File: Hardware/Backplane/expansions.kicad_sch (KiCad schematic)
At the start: 3 parts, among them U101 P2X8C4M64P, U102 TCA9548APWR

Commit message: Adjusts to review comments
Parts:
- C101: Digikey Part No (none) -> 399-C0603C104M4RACTUCT-ND
- renumbered U101 to U2901
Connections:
- net I2C1_{SCL}: now also U102.5 (SC0); no longer U102.7 (SC1)
- net I2C1_{SDA}: now also U102.4 (SD0); no longer U102.6 (SD1)
- net I2C2_{SCL}: now also U102.7 (SC1); no longer U102.9 (SC2)
- net I2C2_{SDA}: now also U102.6 (SD1); no longer U102.8 (SD2)
- net I2C3_{SCL}: now also U102.9 (SC2); no longer U102.11 (SC3)
- net I2C3_{SDA}: now also U102.8 (SD2); no longer U102.10 (SD3)
- net I2C4_{SCL}: now also U102.11 (SC3); no longer U102.14 (SC4)
- net I2C4_{SDA}: now also U102.10 (SD3); no longer U102.13 (SD4)
- net I2C5_{SCL}: now also U102.14 (SC4); no longer U102.16 (SC5)
- net I2C5_{SDA}: now also U102.13 (SD4); no longer U102.15 (SD5)
- net I2C6_{SCL}: now also U102.16 (SC5); no longer U102.18 (SC6)
- net I2C6_{SDA}: now also U102.15 (SD5); no longer U102.17 (SD6)
- net I2C7_{SCL}: now also U102.18 (SC6); no longer U102.20 (SC7)
- net I2C7_{SDA}: now also U102.17 (SD6); no longer U102.19 (SD7)
- net I2C^{BRD}_{SCL}: now also U102.19 (SD7); no longer U102.4 (SD0)
- net I2C^{BRD}_{SDA}: now also U102.20 (SC7); no longer U102.5 (SC0)
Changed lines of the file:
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@@
 	(wire
 		(pts
+			(xy 164.465 152.4) (xy 166.37 152.4)
+		)
+		(stroke
+			(width 0)
+			(type default)
+		)
+	)
+	(wire
+		(pts
 			(xy 37.465 73.66) (xy 37.465 72.39)
 		)
@@
 	(wire
 		(pts
-			(xy 166.37 119.38) (xy 155.575 119.38)
+			(xy 166.37 111.76) (xy 155.575 111.76)
 		)
 		(stroke
@@
 	(wire
 		(pts
-			(xy 166.37 134.62) (xy 155.575 134.62)
+			(xy 166.37 127) (xy 155.575 127)
 		)
 		(stroke
@@
 	(wire
 		(pts
-			(xy 166.37 152.4) (xy 155.575 152.4)
+			(xy 166.37 144.78) (xy 155.575 144.78)
 		)
 		(stroke
@@
 	(wire
 		(pts
-			(xy 166.37 114.3) (xy 155.575 114.3)
+			(xy 166.37 106.68) (xy 155.575 106.68)
 		)
 		(stroke
@@
 	(wire
 		(pts
-			(xy 166.37 127) (xy 155.575 127)
+			(xy 166.37 119.38) (xy 155.575 119.38)
 		)
 		(stroke
@@
 	(wire
 		(pts
-			(xy 166.37 144.78) (xy 155.575 144.78)
+			(xy 166.37 137.16) (xy 155.575 137.16)
 		)
 		(stroke
@@
 	(wire
 		(pts
-			(xy 166.37 149.86) (xy 155.575 149.86)
+			(xy 166.37 142.24) (xy 155.575 142.24)
 		)
 		(stroke
@@
 	(wire
 		(pts
+			(xy 164.465 149.86) (xy 166.37 149.86)
+		)
+		(stroke
+			(width 0)
+			(type default)
+		)
+	)
+	(wire
+		(pts
 			(xy 44.45 35.56) (xy 46.99 35.56)
 		)
@@
 	(wire
 		(pts
-			(xy 166.37 106.68) (xy 155.575 106.68)
+			(xy 166.37 99.06) (xy 155.575 99.06)
 		)
 		(stroke
@@
 	(wire
 		(pts
-			(xy 166.37 111.76) (xy 155.575 111.76)
+			(xy 166.37 104.14) (xy 155.575 104.14)
 		)
 		(stroke
@@
 	(wire
 		(pts
-			(xy 166.37 129.54) (xy 155.575 129.54)
+			(xy 166.37 121.92) (xy 155.575 121.92)
 		)
 		(stroke
@@
 	(wire
 		(pts
-			(xy 166.37 142.24) (xy 155.575 142.24)
+			(xy 166.37 134.62) (xy 155.575 134.62)
 		)
 		(stroke
@@
 	(wire
 		(pts
-			(xy 166.37 121.92) (xy 155.575 121.92)
+			(xy 166.37 114.3) (xy 155.575 114.3)
 		)
 		(stroke
@@
 	(wire
 		(pts
-			(xy 166.37 137.16) (xy 155.575 137.16)
+			(xy 166.37 129.54) (xy 155.575 129.54)
 		)
 		(stroke
@@
 	(wire
 		(pts
-			(xy 166.37 104.14) (xy 155.575 104.14)
+			(xy 166.37 96.52) (xy 155.575 96.52)
 		)
 		(stroke
@@
 	)
 	(label "I2C7_{SCL}"
-		(at 155.575 152.4 0)
+		(at 155.575 144.78 0)
 		(effects
 			(font
@@
 	)
 	(label "I2C7_{SDA}"
-		(at 155.575 149.86 0)
+		(at 155.575 142.24 0)
 		(effects
 			(font
@@
 	)
 	(label "I2C2_{SCL}"
-		(at 155.575 114.3 0)
+		(at 155.575 106.68 0)
 		(effects
 			(font
@@
 	)
 	(label "I2C6_{SCL}"
-		(at 155.575 144.78 0)
+		(at 155.575 137.16 0)
 		(effects
 			(font
@@
 	)
 	(label "I2C3_{SDA}"
-		(at 155.575 119.38 0)
+		(at 155.575 111.76 0)
 		(effects
 			(font
@@
 	)
 	(label "I2C1_{SCL}"
-		(at 155.575 106.68 0)
+		(at 155.575 99.06 0)
 		(effects
 			(font
@@
 	)
 	(label "I2C4_{SCL}"
-		(at 155.575 129.54 0)
+		(at 155.575 121.92 0)
 		(effects
 			(font
@@
 	)
 	(label "I2C3_{SCL}"
-		(at 155.575 121.92 0)
+		(at 155.575 114.3 0)
 		(effects
 			(font
@@
 	)
 	(label "I2C4_{SDA}"
-		(at 155.575 127 0)
+		(at 155.575 119.38 0)
 		(effects
 			(font
@@
 	)
 	(label "I2C2_{SDA}"
-		(at 155.575 111.76 0)
+		(at 155.575 104.14 0)
 		(effects
 			(font
@@
 	)
 	(label "I2C1_{SDA}"
-		(at 155.575 104.14 0)
+		(at 155.575 96.52 0)
 		(effects
 			(font
@@
 	)
 	(label "I2C6_{SDA}"
-		(at 155.575 142.24 0)
+		(at 155.575 134.62 0)
 		(effects
 			(font
@@
 	)
 	(label "I2C5_{SDA}"
-		(at 155.575 134.62 0)
+		(at 155.575 127 0)
 		(effects
 			(font
@@
 	)
 	(label "I2C5_{SCL}"
-		(at 155.575 137.16 0)
+		(at 155.575 129.54 0)
 		(effects
 			(font
@@
 	(global_label "I2C^{BRD}_{SDA}"
 		(shape input)
-		(at 166.37 99.06 180)
+		(at 164.465 152.4 180)
 		(fields_autoplaced yes)
 		(effects
@@
 		)
 		(property "Intersheetrefs" "${INTERSHEET_REFS}"
-			(at 154.3472 99.06 0)
+			(at 152.4422 152.4 0)
 			(effects
 				(font
@@
 	(global_label "I2C^{BRD}_{SCL}"
 		(shape input)
-		(at 166.37 96.52 180)
+		(at 164.465 149.86 180)
 		(fields_autoplaced yes)
 		(effects
@@
 		)
 		(property "Intersheetrefs" "${INTERSHEET_REFS}"
-			(at 154.3956 96.52 0)
+			(at 152.4906 149.86 0)
 			(effects
 				(font
@@
 		(on_board yes)
 		(dnp no)
-		(property "Reference" "U101"
+		(property "Reference" "U2901"
 			(at 251.46 17.78 0)
 			(effects
@@
 			(project "Backplane"
 				(path "/c6da991a-d3ed-4ac1-8b0d-12cd7ba8539b/fc524bed-e1de-43ff-9b23-75610ded7ea1"
-					(reference "U101")
+					(reference "U2901")
 					(unit 1)
 				)
@@
 			)
 		)
-		(property "Datasheet" ""
+		(property "Datasheet" "https://www.yageogroup.com/content/datasheet/asset/file/KEM_C1002_X7R_SMD"
 			(at 202.565 125.095 0)
 			(effects
@@
 			(at 202.565 125.095 0)
 			(effects
+				(font
+					(size 1.27 1.27)
+				)
+				(hide yes)
+			)
+		)
+		(property "Digikey Part No" "399-C0603C104M4RACTUCT-ND"
+			(at 202.565 125.095 0)
+			(effects

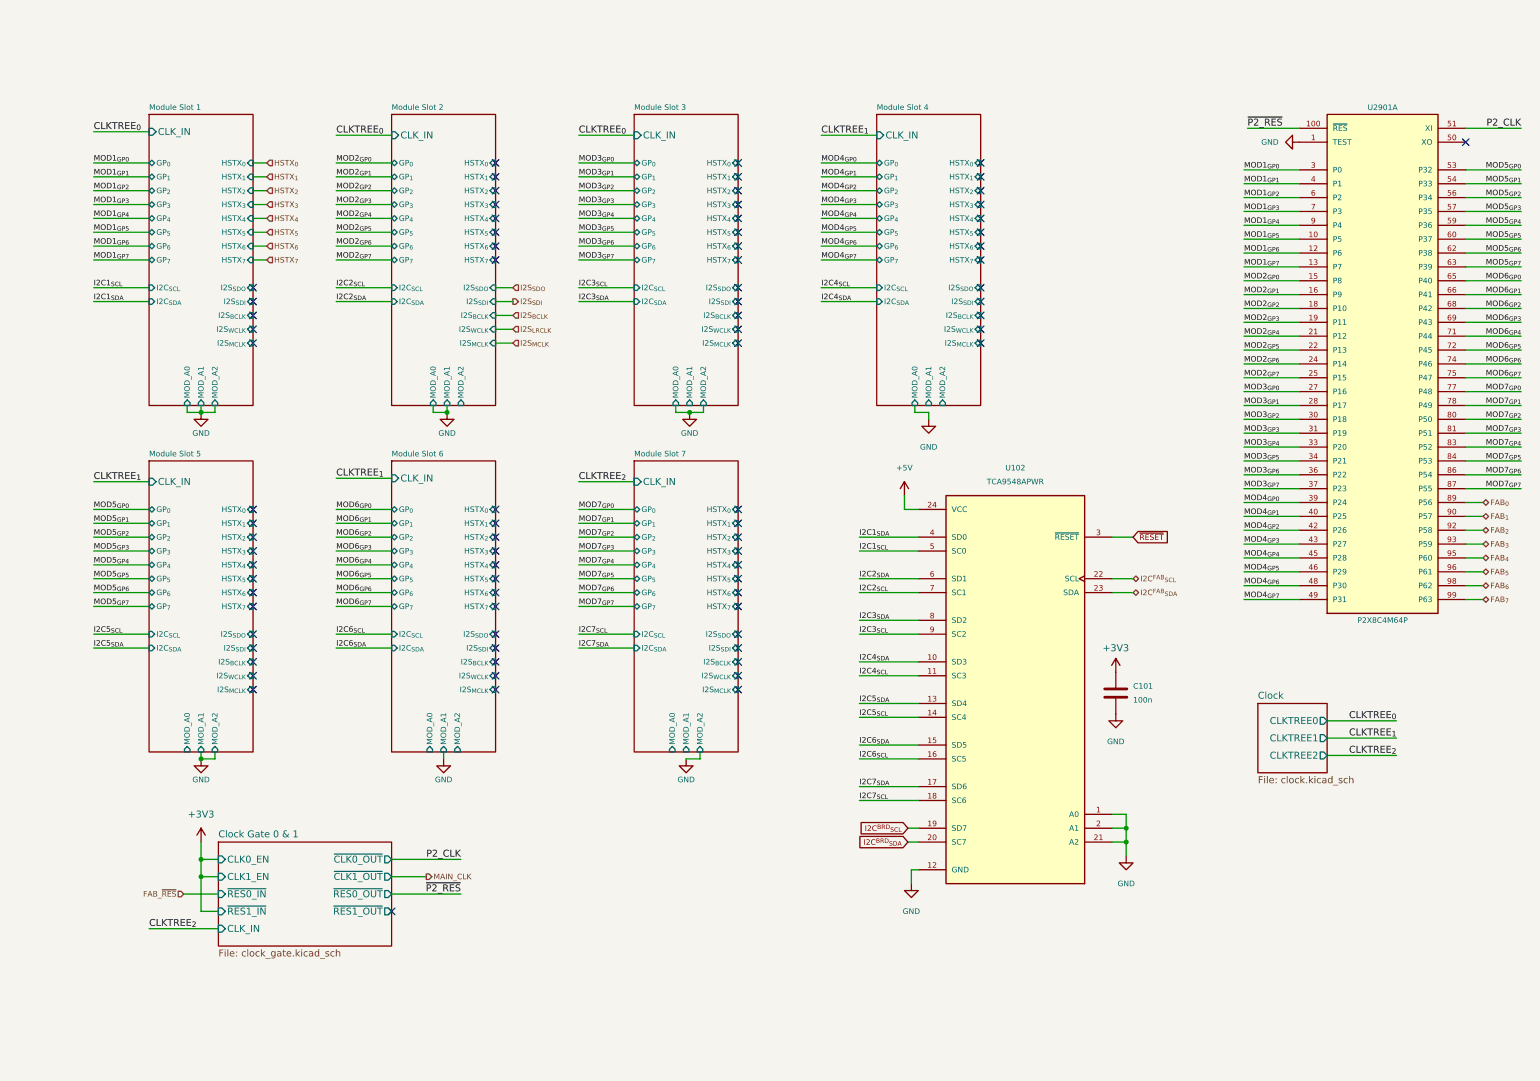
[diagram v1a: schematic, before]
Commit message: Cleans up Backplane schematic even more. Less parts in the BOM, less mistakes!
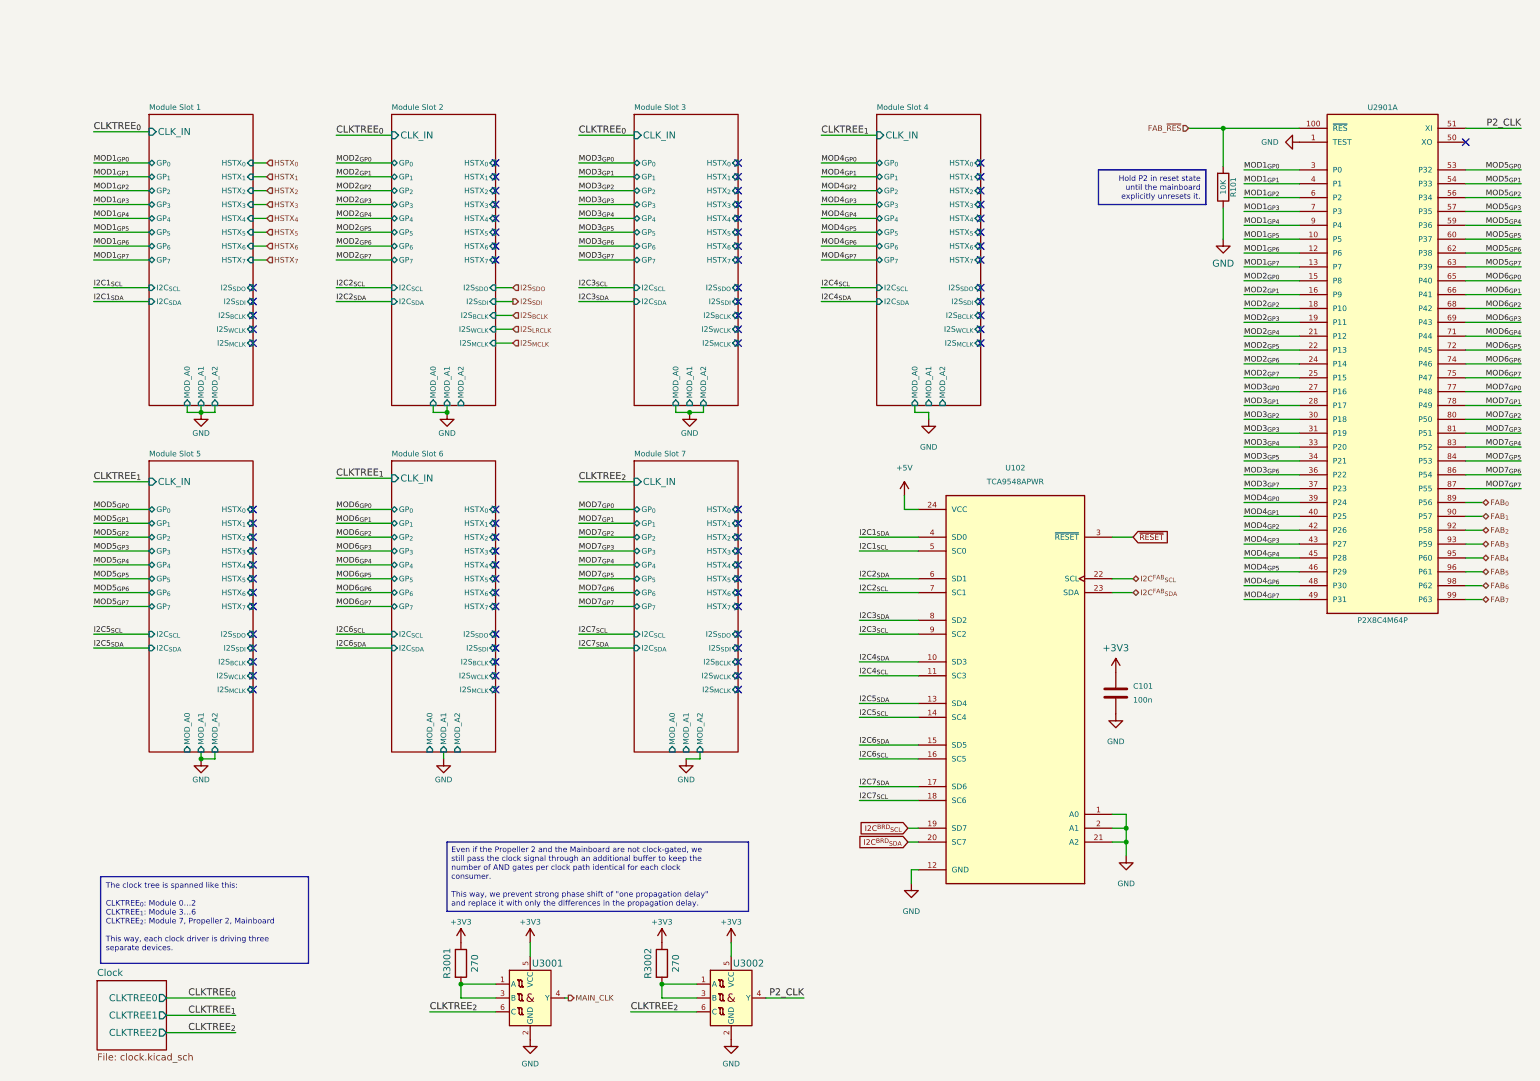
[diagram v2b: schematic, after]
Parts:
- added R101: 10K, Resistor_SMD:R_0603_1608Metric, symbol Device:R
- added R3001, R3002: 270, Resistor_SMD:R_0603_1608Metric, symbol Device:R
- added U3001, U3002: NL17SZS11DFT2G-Q, Package_TO_SOT_SMD:SOT-363_SC-70-6, symbol Home Computer:NL17SZS11DFT2G-Q
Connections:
- net ~{P2_RES} is gone; now on net FAB_~{RES}: U2901.100 (~{RES})
- net +3V3: now also R3001.1, R3002.1, U3001.5 (VCC), U3002.5 (VCC)
- net CLKTREE_{2}: now also U3001.6 (C), U3002.6 (C)
- net FAB_~{RES}: now also R101.2
- net GND: now also R101.1, U3001.2 (GND), U3002.2 (GND)
- net MAIN_CLK: now also U3001.4 (Y)
- net P2_CLK: now also U3002.4 (Y)
- new net: R3001.2, U3001.1 (A), U3001.3 (B)
- new net: R3002.2, U3002.1 (A), U3002.3 (B)
- no-connect marks 80 -> 79
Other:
- removed sheet Clock Gate 0 & 1

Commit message: Finally renames all modules from MOD1…7 into MOD0…6
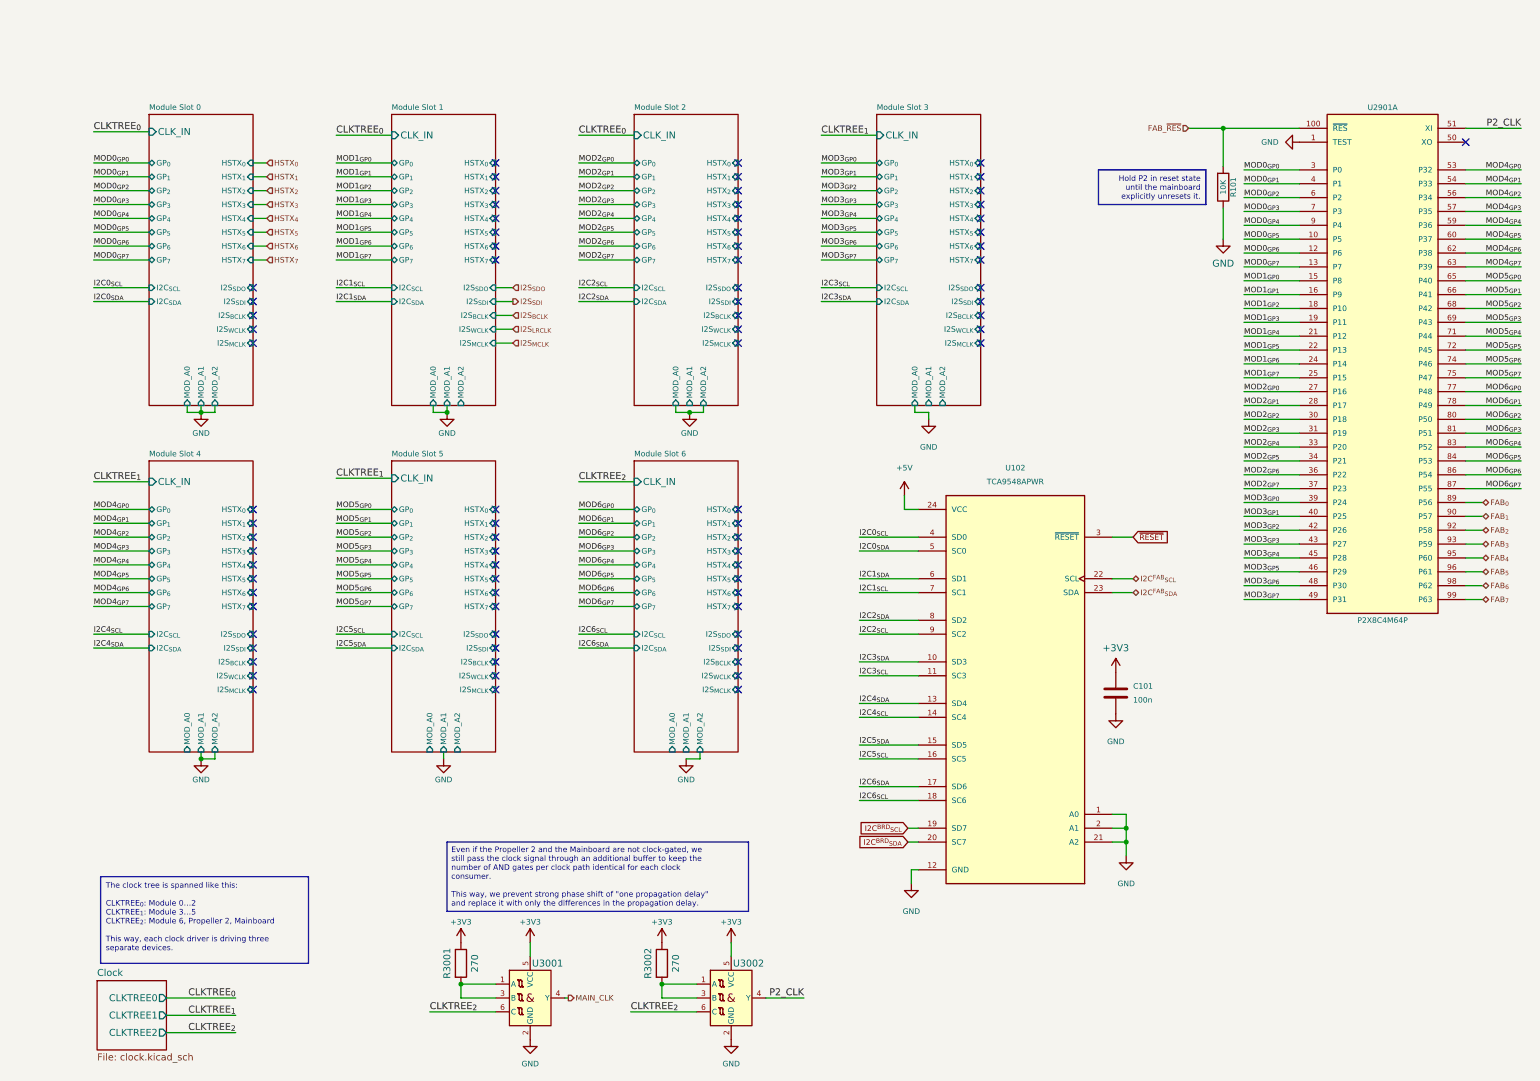
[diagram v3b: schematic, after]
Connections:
- net I2C7_{SCL} is gone; now on net I2C6_{SCL}: U102.18 (SC6)
- net I2C7_{SDA} is gone; now on net I2C6_{SDA}: U102.17 (SD6)
- net MOD7_{GP0} is gone; now on net MOD6_{GP0}: U2901.77 (P48)
- net MOD7_{GP1} is gone; now on net MOD6_{GP1}: U2901.78 (P49)
- net MOD7_{GP2} is gone; now on net MOD6_{GP2}: U2901.80 (P50)
- net MOD7_{GP3} is gone; now on net MOD6_{GP3}: U2901.81 (P51)
- net MOD7_{GP4} is gone; now on net MOD6_{GP4}: U2901.83 (P52)
- net MOD7_{GP5} is gone; now on net MOD6_{GP5}: U2901.84 (P53)
- net MOD7_{GP6} is gone; now on net MOD6_{GP6}: U2901.86 (P54)
- net MOD7_{GP7} is gone; now on net MOD6_{GP7}: U2901.87 (P55)
- net I2C1_{SCL}: now also U102.7 (SC1); no longer U102.5 (SC0)
- net I2C1_{SDA}: now also U102.6 (SD1); no longer U102.4 (SD0)
- net I2C2_{SCL}: now also U102.9 (SC2); no longer U102.7 (SC1)
- net I2C2_{SDA}: now also U102.8 (SD2); no longer U102.6 (SD1)
- net I2C3_{SCL}: now also U102.11 (SC3); no longer U102.9 (SC2)
- net I2C3_{SDA}: now also U102.10 (SD3); no longer U102.8 (SD2)
- net I2C4_{SCL}: now also U102.14 (SC4); no longer U102.11 (SC3)
- net I2C4_{SDA}: now also U102.13 (SD4); no longer U102.10 (SD3)
- net I2C5_{SCL}: now also U102.16 (SC5); no longer U102.14 (SC4)
- net I2C5_{SDA}: now also U102.15 (SD5); no longer U102.13 (SD4)
- net I2C6_{SCL}: no longer U102.16 (SC5)
- net I2C6_{SDA}: no longer U102.15 (SD5)
- net MOD1_{GP0}: now also U2901.15 (P8); no longer U2901.3 (P0)
- net MOD1_{GP1}: now also U2901.16 (P9); no longer U2901.4 (P1)
- net MOD1_{GP2}: now also U2901.18 (P10); no longer U2901.6 (P2)
- net MOD1_{GP3}: now also U2901.19 (P11); no longer U2901.7 (P3)
- net MOD1_{GP4}: now also U2901.21 (P12); no longer U2901.9 (P4)
- net MOD1_{GP5}: now also U2901.22 (P13); no longer U2901.10 (P5)
- net MOD1_{GP6}: now also U2901.24 (P14); no longer U2901.12 (P6)
- net MOD1_{GP7}: now also U2901.25 (P15); no longer U2901.13 (P7)
- net MOD2_{GP0}: now also U2901.27 (P16); no longer U2901.15 (P8)
- net MOD2_{GP1}: now also U2901.28 (P17); no longer U2901.16 (P9)
- net MOD2_{GP2}: now also U2901.30 (P18); no longer U2901.18 (P10)
- net MOD2_{GP3}: now also U2901.31 (P19); no longer U2901.19 (P11)
- net MOD2_{GP4}: now also U2901.33 (P20); no longer U2901.21 (P12)
- net MOD2_{GP5}: now also U2901.34 (P21); no longer U2901.22 (P13)
- net MOD2_{GP6}: now also U2901.36 (P22); no longer U2901.24 (P14)
- net MOD2_{GP7}: now also U2901.37 (P23); no longer U2901.25 (P15)
- net MOD3_{GP0}: now also U2901.39 (P24); no longer U2901.27 (P16)
- net MOD3_{GP1}: now also U2901.40 (P25); no longer U2901.28 (P17)
- net MOD3_{GP2}: now also U2901.42 (P26); no longer U2901.30 (P18)
- net MOD3_{GP3}: now also U2901.43 (P27); no longer U2901.31 (P19)
- net MOD3_{GP4}: now also U2901.45 (P28); no longer U2901.33 (P20)
- net MOD3_{GP5}: now also U2901.46 (P29); no longer U2901.34 (P21)
- net MOD3_{GP6}: now also U2901.48 (P30); no longer U2901.36 (P22)
- net MOD3_{GP7}: now also U2901.49 (P31); no longer U2901.37 (P23)
- net MOD4_{GP0}: now also U2901.53 (P32); no longer U2901.39 (P24)
- net MOD4_{GP1}: now also U2901.54 (P33); no longer U2901.40 (P25)
- net MOD4_{GP2}: now also U2901.56 (P34); no longer U2901.42 (P26)
- net MOD4_{GP3}: now also U2901.57 (P35); no longer U2901.43 (P27)
- net MOD4_{GP4}: now also U2901.59 (P36); no longer U2901.45 (P28)
- net MOD4_{GP5}: now also U2901.60 (P37); no longer U2901.46 (P29)
- net MOD4_{GP6}: now also U2901.62 (P38); no longer U2901.48 (P30)
- net MOD4_{GP7}: now also U2901.63 (P39); no longer U2901.49 (P31)
- net MOD5_{GP0}: now also U2901.65 (P40); no longer U2901.53 (P32)
- net MOD5_{GP1}: now also U2901.66 (P41); no longer U2901.54 (P33)
- net MOD5_{GP2}: now also U2901.68 (P42); no longer U2901.56 (P34)
- net MOD5_{GP3}: now also U2901.69 (P43); no longer U2901.57 (P35)
- net MOD5_{GP4}: now also U2901.71 (P44); no longer U2901.59 (P36)
- net MOD5_{GP5}: now also U2901.72 (P45); no longer U2901.60 (P37)
- net MOD5_{GP6}: now also U2901.74 (P46); no longer U2901.62 (P38)
- net MOD5_{GP7}: now also U2901.75 (P47); no longer U2901.63 (P39)
- net MOD6_{GP0}: no longer U2901.65 (P40)
- net MOD6_{GP1}: no longer U2901.66 (P41)
- net MOD6_{GP2}: no longer U2901.68 (P42)
- net MOD6_{GP3}: no longer U2901.69 (P43)
- net MOD6_{GP4}: no longer U2901.71 (P44)
- net MOD6_{GP5}: no longer U2901.72 (P45)
- net MOD6_{GP6}: no longer U2901.74 (P46)
- net MOD6_{GP7}: no longer U2901.75 (P47)
- new net I2C0_{SCL}: U102.4 (SD0)
- new net I2C0_{SDA}: U102.5 (SC0)
- new net MOD0_{GP0}: U2901.3 (P0)
- new net MOD0_{GP1}: U2901.4 (P1)
- new net MOD0_{GP2}: U2901.6 (P2)
- new net MOD0_{GP3}: U2901.7 (P3)
- new net MOD0_{GP4}: U2901.9 (P4)
- new net MOD0_{GP5}: U2901.10 (P5)
- new net MOD0_{GP6}: U2901.12 (P6)
- new net MOD0_{GP7}: U2901.13 (P7)
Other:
- removed sheet Module Slot 7
- added sheet Module Slot 0 (module_slot.kicad_sch)
